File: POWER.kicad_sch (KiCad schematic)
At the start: 0 parts

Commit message: added micro and 3 sensors and connectors with USB
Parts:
- added C16: 100nF 25V, Capacitor_SMD:C_0603_1608Metric, symbol Device:C
- added C17: 75pF, Capacitor_SMD:C_0603_1608Metric, symbol Device:C
- added C18, C19: 22uF 25V, Capacitor_SMD:C_1206_3216Metric, symbol Device:C
- added C6: 10uF 25V, Capacitor_SMD:C_1206_3216Metric, symbol Device:C
- added C7: 100nF, Capacitor_SMD:C_0603_1608Metric, symbol Device:C
- added C8: 1uF 16V, Capacitor_SMD:C_0603_1608Metric, symbol Device:C
- added C9: 1uF 10V, Capacitor_SMD:C_0603_1608Metric, symbol Device:C
- added L1: L, symbol Device:L
- added R2: 100k 1%, Resistor_SMD:R_0603_1608Metric, symbol Device:R
- added R3: 13.3k 1%, Resistor_SMD:R_0603_1608Metric, symbol Device:R
- added TP4: 5V0, symbol Connector:TestPoint
- added TP5: 3V3, symbol Connector:TestPoint
- added U2: TPS54302, Package_TO_SOT_SMD:SOT-23-6, symbol Regulator_Switching:TPS54308
- added U3: AP2112K-3.3, Package_TO_SOT_SMD:SOT-23-5, symbol Regulator_Linear:AP2112K-3.3
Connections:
- new net: C7.2, L1.1, U2.2 (SW)
- new net: R2.2, R3.1, U2.4 (FB)
- new net: C7.1, U2.6 (BOOT)
- new net +BATT: C16.1, C6.1, U2.3 (VIN)
- new net 3V3: C9.1, TP5.1, U3.5 (VOUT)
- new net 5V0: C17.1, C18.1, C19.1, C8.1, L1.2, R2.1, TP4.1, U3.1 (VIN), U3.3 (EN)
- new net GND: C16.2, C17.2, C18.2, C19.2, C6.2, C8.2, C9.2, R3.2, U2.1 (GND), U3.2 (GND)
- no-connect marks 0 -> 1
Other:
- note added: "3.3V LDO"
- note added: "5V Buck"

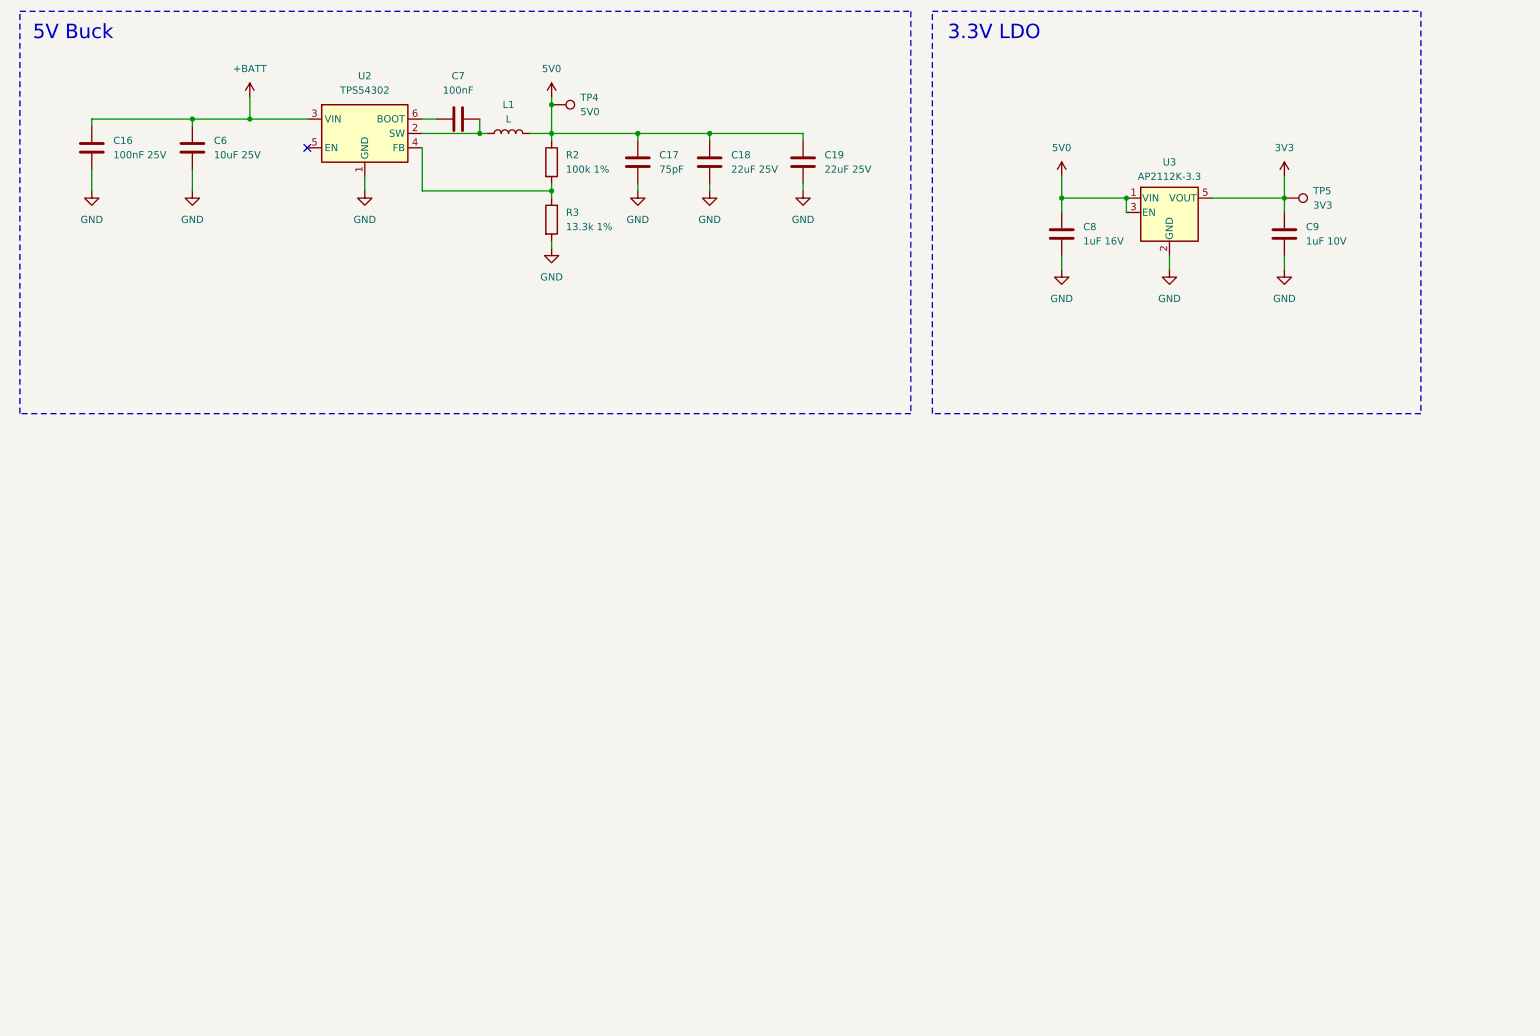
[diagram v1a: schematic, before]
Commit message: added Buzzer, status LEDs
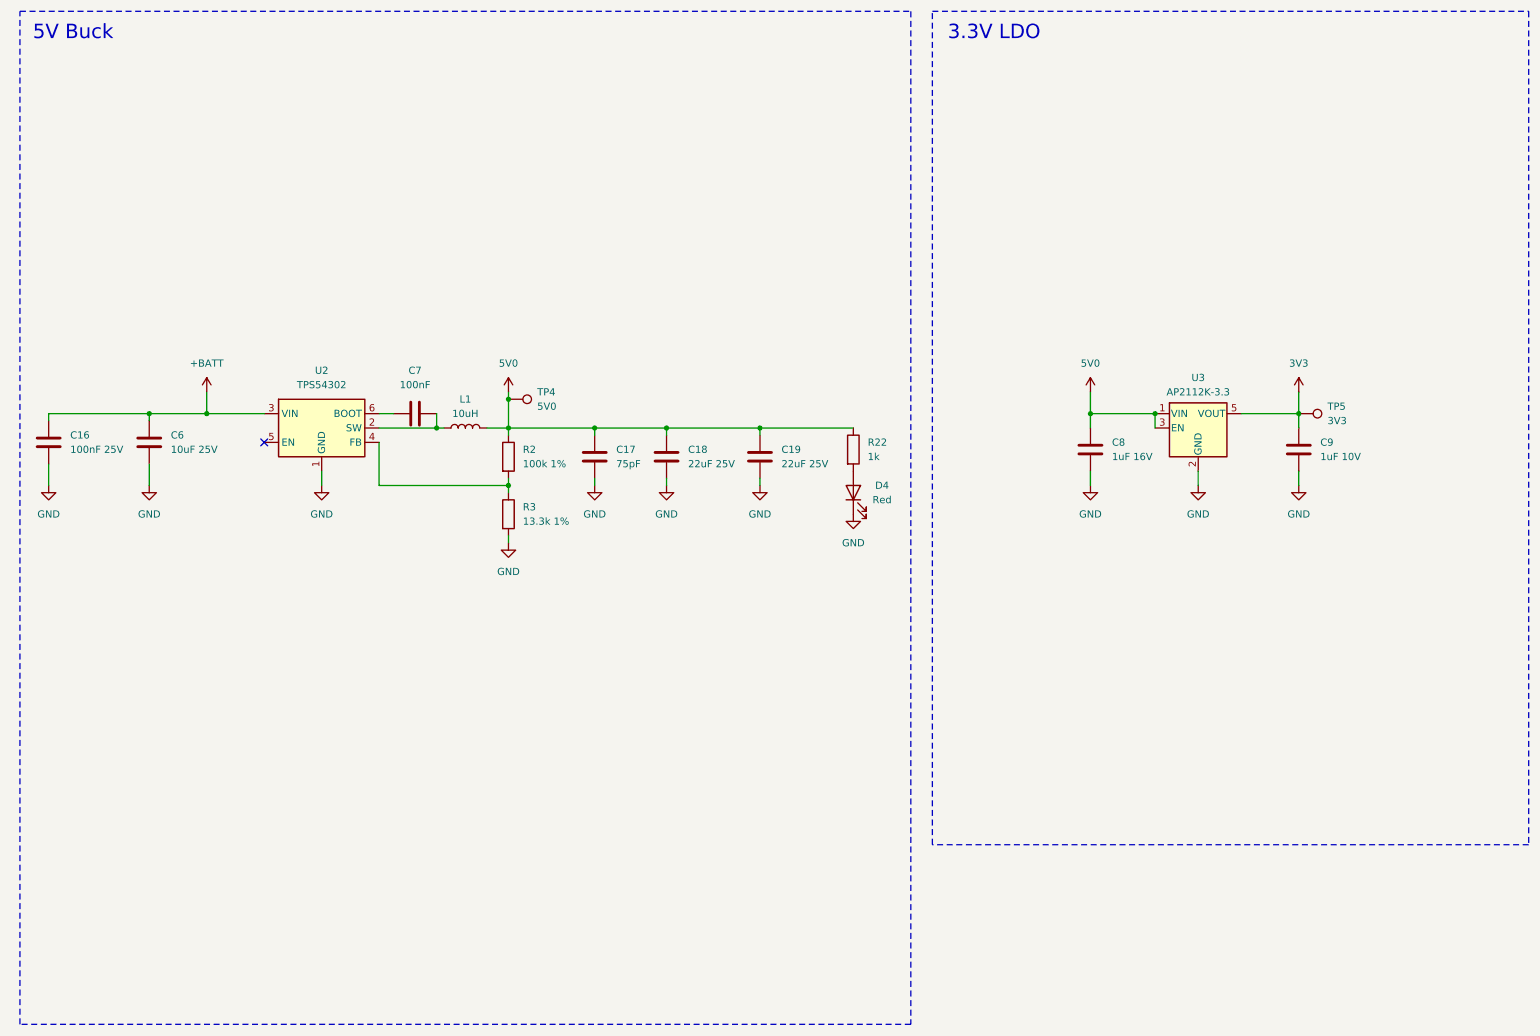
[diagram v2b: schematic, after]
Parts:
- added D4: Red, LED_SMD:LED_0603_1608Metric, symbol Device:LED
- added R22: 1k, Resistor_SMD:R_0603_1608Metric, symbol Device:R
- L1: value L -> 10uH; footprint (none) -> Inductor_SMD:L_Wuerth_XHMI-6060; MPN (none) -> 74439346100
- TP4, TP5: footprint (none) -> TestPoint:TestPoint_Pad_D1.5mm
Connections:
- net 5V0: now also R22.1
- net GND: now also D4.1 (K)
- new net: D4.2 (A), R22.2
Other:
- moved on the sheet: C16, C17, C18, C19, C6, C7, C8, C9, L1, R2, R3, TP4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

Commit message: Battery protection, camera switch, 64MB flash, ERC clean
- Fuse + TVS on battery input, camera load switch (TPS22917)
- Flash to W25Q512JVFIQ (SOIC-16), hand-solder passive footprints
- Power LED, title blocks, U5 footprint, PWR/NC flags (0 ERC)
- Regenerated schematic PDF
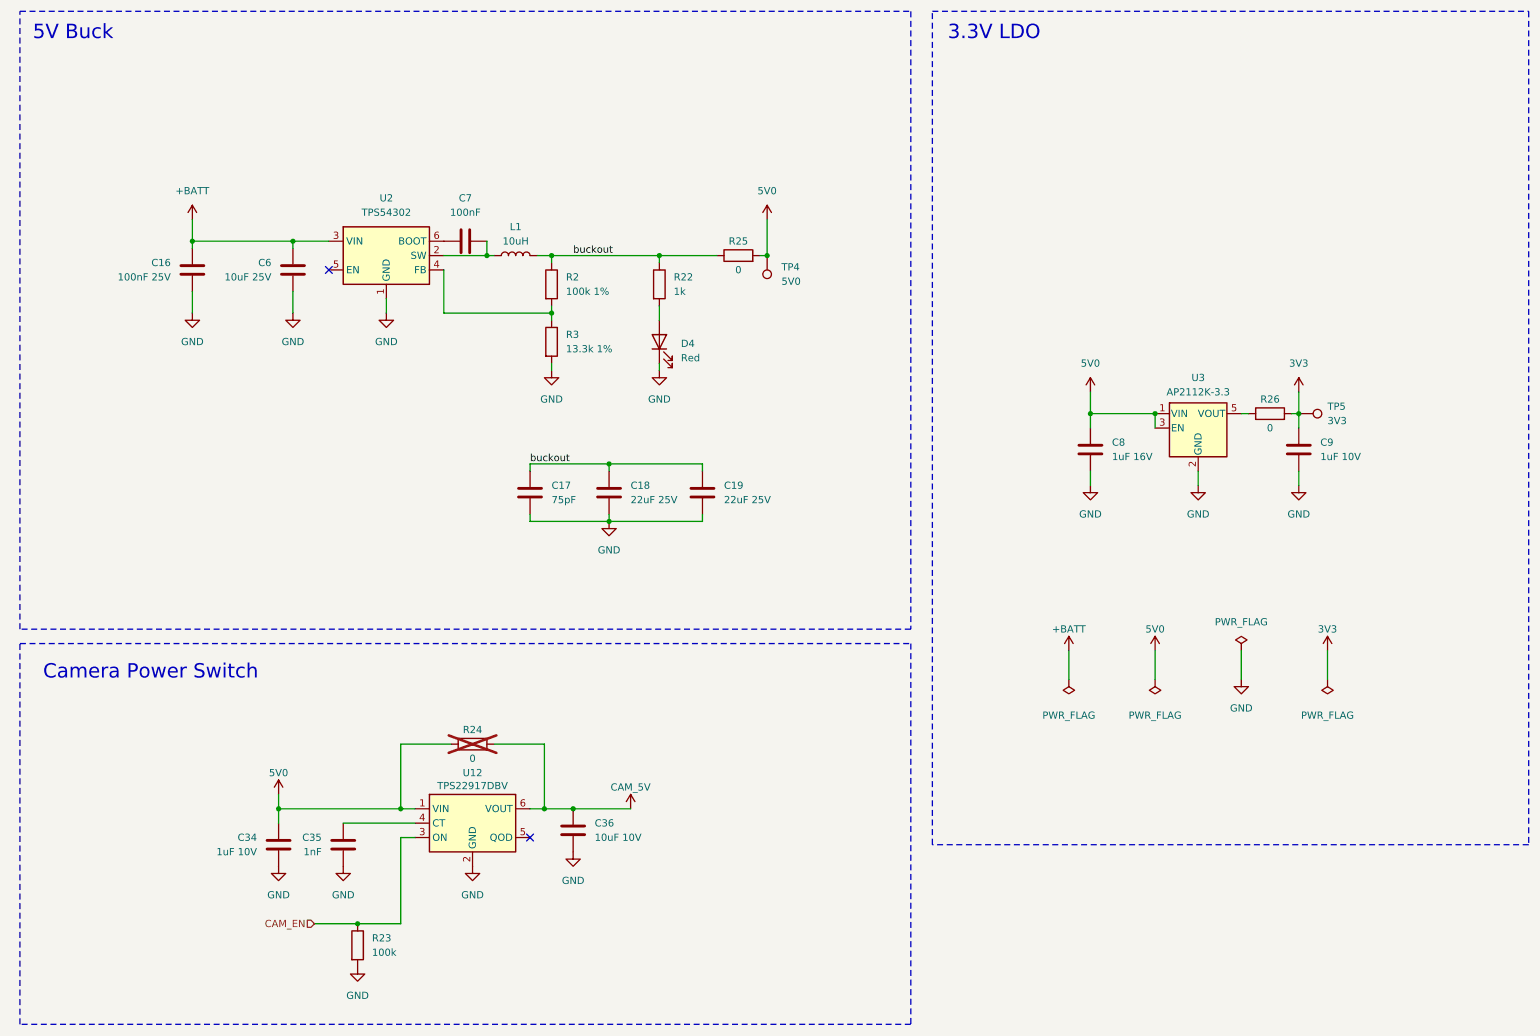
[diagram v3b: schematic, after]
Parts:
- added C34: 1uF 10V, Capacitor_SMD:C_0603_1608Metric_Pad1.08x0.95mm_HandSolder, symbol Device:C
- added C35: 1nF, Capacitor_SMD:C_0603_1608Metric_Pad1.08x0.95mm_HandSolder, symbol Device:C
- added C36: 10uF 10V, Capacitor_SMD:C_0805_2012Metric_Pad1.18x1.45mm_HandSolder, symbol Device:C
- added R23: 100k, Resistor_SMD:R_0603_1608Metric_Pad0.98x0.95mm_HandSolder, symbol Device:R
- added R24, R25, R26: 0, Resistor_SMD:R_0603_1608Metric_Pad0.98x0.95mm_HandSolder, symbol Device:R
- added U12: TPS22917DBV, Package_TO_SOT_SMD:SOT-23-6, symbol Power_Management:TPS22917DBV
- C16, C17, C7, C8, C9: footprint Capacitor_SMD:C_0603_1608Metric -> Capacitor_SMD:C_0603_1608Metric_Pad1.08x0.95mm_HandSolder
- C18, C19, C6: footprint Capacitor_SMD:C_1206_3216Metric -> Capacitor_SMD:C_1206_3216Metric_Pad1.33x1.80mm_HandSolder
- D4: footprint LED_SMD:LED_0603_1608Metric -> LED_SMD:LED_0603_1608Metric_Pad1.05x0.95mm_HandSolder
- R2, R22, R3: footprint Resistor_SMD:R_0603_1608Metric -> Resistor_SMD:R_0603_1608Metric_Pad0.98x0.95mm_HandSolder
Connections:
- net 3V3: now also R26.2; no longer U3.5 (VOUT)
- net 5V0: now also C34.1, R24.1, R25.2, U12.1 (VIN); no longer C17.1, C18.1, C19.1, L1.2, R2.1, R22.1
- net GND: now also C34.2, C35.2, C36.2, R23.2, U12.2 (GND)
- new net: C35.1, U12.4 (CT)
- new net: R26.1, U3.5 (VOUT)
- new net CAM_5V: C36.1, R24.2, U12.6 (VOUT)
- new net CAM_EN: R23.1, U12.3 (ON)
- new net buckout: C17.1, C18.1, C19.1, L1.2, R2.1, R22.1, R25.1
- no-connect marks 1 -> 2
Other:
- note added: "Camera Power Switch"
- title: (none) -> Power: Battery, 5V Buck, 3.3V LDO
- moved on the sheet: C16, C6, C7, L1, R2, R3, U2
